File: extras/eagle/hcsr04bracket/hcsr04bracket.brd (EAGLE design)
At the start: 30.5 x 30.5 mm, 11 parts

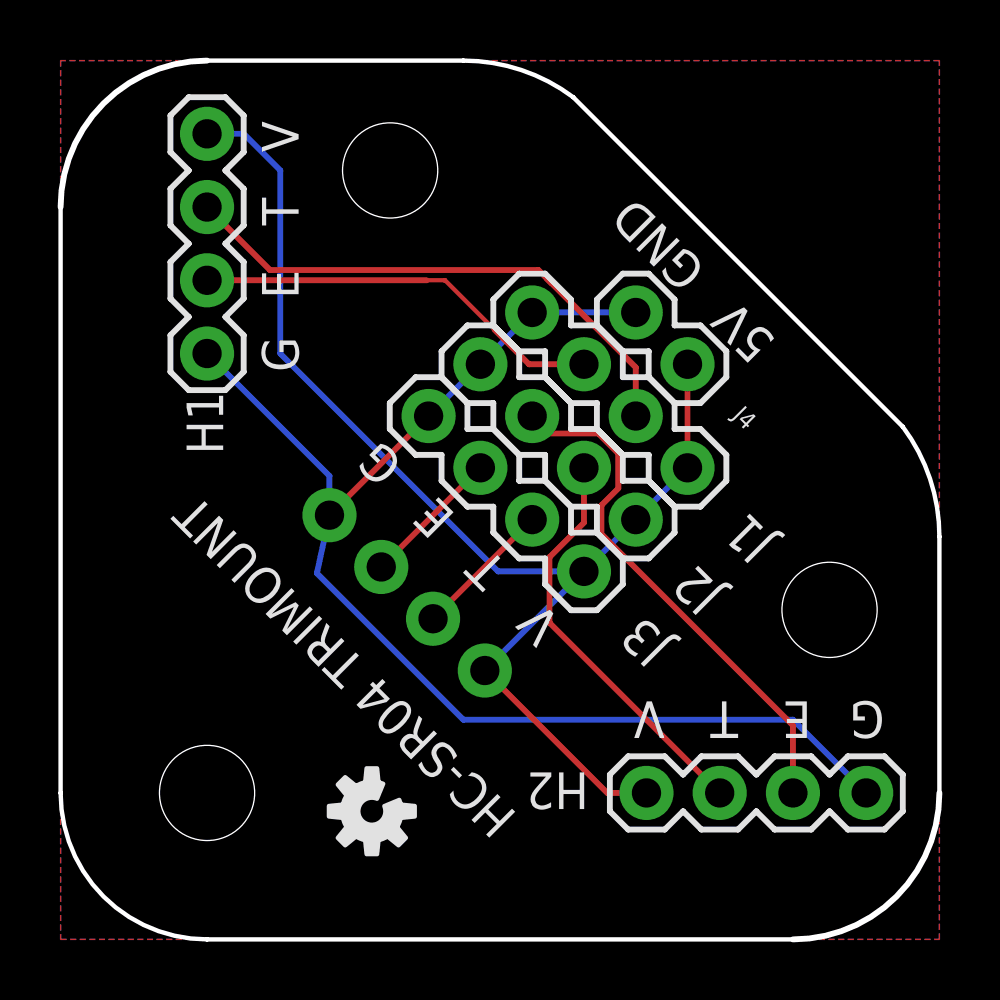
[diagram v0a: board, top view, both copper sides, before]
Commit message: 1.2.0 eagle files and examples updated
Eagle files updated for OctoSonarX2 and Trimounts to reflect modifications between prototype and production.

OctoSonarX2 - tweaked bypass caps. Rerouted 5V with wider traces.
Examples - tidies up with serial only tests and separate LCD tests.
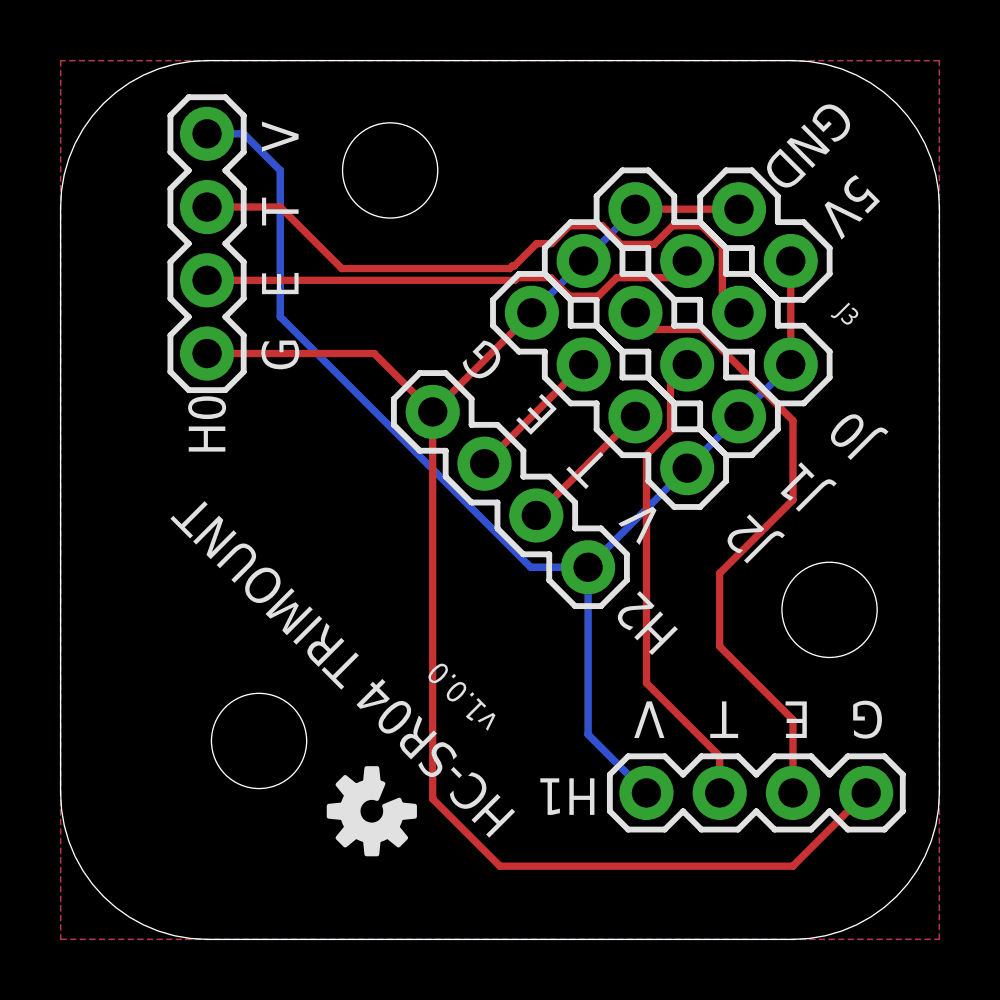
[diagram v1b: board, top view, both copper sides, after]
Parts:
- removed H3: (no value), mystuff:1X04
- removed J4: (no value), SparkFun-Connectors:1X02
- added H0: H0, mystuff:1X04
- added J0: J0, mystuff:1X04
- H1: value (none) -> H1; device SparkFun-Connectors:1X04 -> mystuff:1X04
- H2: value (none) -> H2; device SparkFun-Connectors:1X04 -> mystuff:1X04
- J1: value (none) -> J1; device SparkFun-Connectors:1X04 -> mystuff:1X04
- J2: value (none) -> J2; device SparkFun-Connectors:1X04 -> mystuff:1X04
- J3: device SparkFun-Connectors:1X04 -> SparkFun-Connectors:1X02
- moved H1 27.5 mm to (20.3, 5.08), flipped to the bottom, turned to 180 degrees
- moved J3 12.9 mm to (25.3, 23.5)
- moved H2 8.08 mm to (18.3, 12.9), turned to 135 degrees
- moved U$3 2.55 mm to (6.88, 6.88)
- moved J2 2.52 mm to (21.7, 16.3)
- moved J1 2.52 mm to (23.5, 18.1)
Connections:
- net E1: now also H1.3, J1.3; no longer H2.3, J2.3
- net E2: now also H0.3, J0.3; no longer H1.3, J1.3
- net E3: now also H2.3, J2.3; no longer H3.3, J3.3
- net GND: now also H0.4, J0.4, J3.2; no longer H3.4, J3.4, J4.2
- net T1: now also H1.2, J1.2; no longer H2.2, J2.2
- net T2: now also H0.2, J0.2; no longer H1.2, J1.2
- net T3: now also H2.2, J2.2; no longer H3.2, J3.2
- net VCC: now also H0.1, J0.1; no longer H3.1, J4.1
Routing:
- net GND: track 45.2 -> 52.7 mm
- net E1: track 18.3 -> 22.0 mm
- net T2: track 19.1 -> 22.7 mm
- net E2: track 14.3 -> 17.5 mm
- net T1: track 14.2 -> 16.5 mm
- net VCC: track 44.0 -> 44.6 mm
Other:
- outline, holes or cut-outs redrawn
- board text added: "github.com/arielnh56/octosonar"
- board text added: "v1.0.0"

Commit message: Revert "Updates to X2 test and trimount bracket"
This reverts commit f0c77c11ce1398fcc169d7c2890869ee86536cf6.
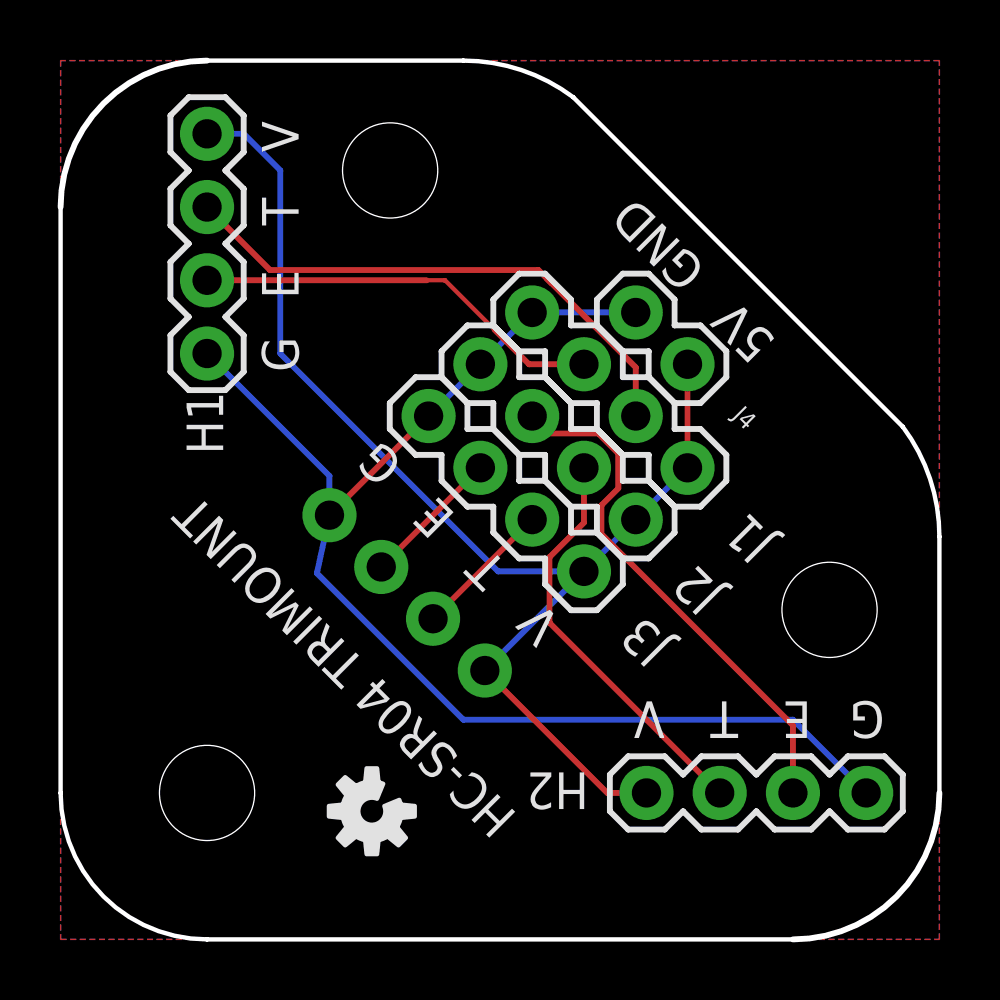
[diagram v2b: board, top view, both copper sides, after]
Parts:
- removed H0: H0, mystuff:1X04
- removed J0: J0, mystuff:1X04
- added H3: (no value), mystuff:1X04
- added J4: (no value), SparkFun-Connectors:1X02
- H1: value H1 -> (none); device mystuff:1X04 -> SparkFun-Connectors:1X04
- H2: value H2 -> (none); device mystuff:1X04 -> SparkFun-Connectors:1X04
- J1: value J1 -> (none); device mystuff:1X04 -> SparkFun-Connectors:1X04
- J2: value J2 -> (none); device mystuff:1X04 -> SparkFun-Connectors:1X04
- J3: device SparkFun-Connectors:1X02 -> SparkFun-Connectors:1X04
- moved H1 27.5 mm to (5.08, 27.9), flipped to the top, turned to 270 degrees
- moved J3 12.9 mm to (18.2, 12.8)
- moved H2 8.08 mm to (20.3, 5.08), turned to 0 degrees
- moved U$3 2.55 mm to (5.08, 5.08)
- moved J2 2.52 mm to (19.9, 14.6)
- moved J1 2.52 mm to (21.7, 16.4)
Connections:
- net E1: now also H2.3, J2.3; no longer H1.3, J1.3
- net E2: now also H1.3, J1.3; no longer H0.3, J0.3
- net E3: now also H3.3, J3.3; no longer H2.3, J2.3
- net GND: now also H3.4, J3.4, J4.2; no longer H0.4, J0.4, J3.2
- net T1: now also H2.2, J2.2; no longer H1.2, J1.2
- net T2: now also H1.2, J1.2; no longer H0.2, J0.2
- net T3: now also H3.2, J3.2; no longer H2.2, J2.2
- net VCC: now also H3.1, J4.1; no longer H0.1, J0.1
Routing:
- net GND: track 52.7 -> 45.2 mm
- net E1: track 22.0 -> 18.3 mm
- net T2: track 22.7 -> 19.1 mm
- net E2: track 17.5 -> 14.3 mm
- net T1: track 16.5 -> 14.2 mm
- net VCC: track 44.6 -> 44.0 mm
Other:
- outline, holes or cut-outs redrawn
- board text removed: "github.com/arielnh56/octosonar"
- board text removed: "v1.0.0"
